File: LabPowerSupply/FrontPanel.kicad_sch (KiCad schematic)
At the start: 27 parts

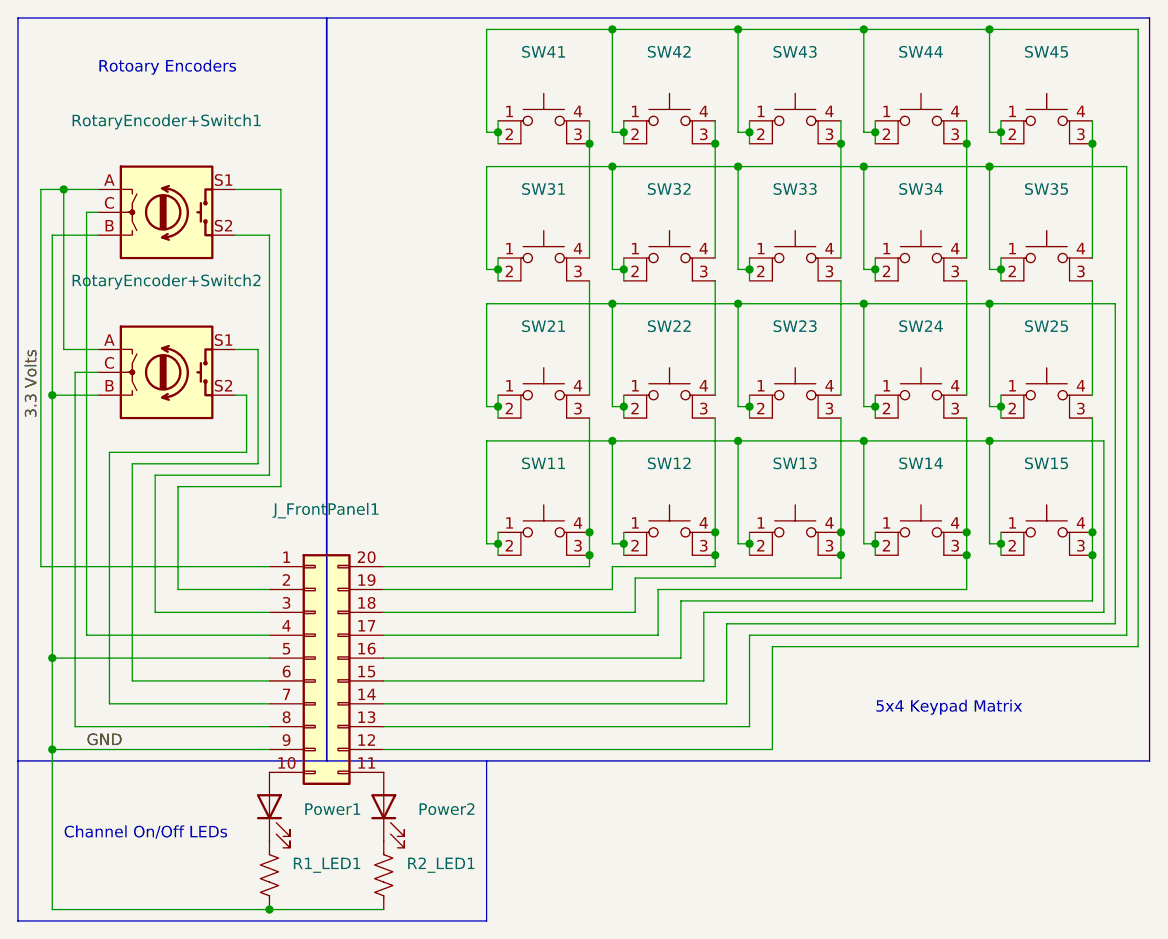
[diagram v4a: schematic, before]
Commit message: Added mcu capacitors, split 5v inductors
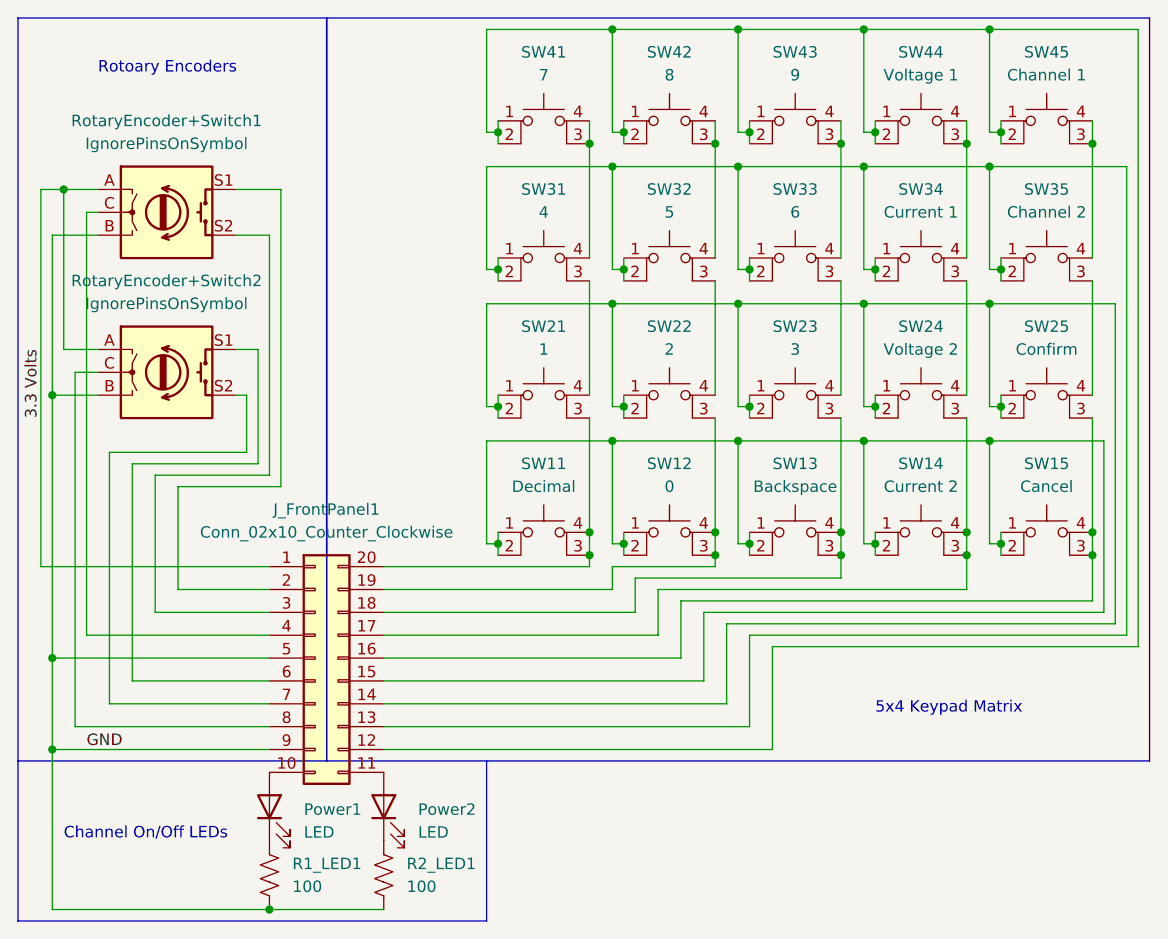
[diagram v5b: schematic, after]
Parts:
- J_FrontPanel1: value (none) -> Conn_02x10_Counter_Clockwise; footprint (none) -> Connector_IDC:IDC-Header_2x10_P2.54mm_Vertical
- Power1, Power2: value (none) -> LED; footprint (none) -> LED_THT:LED_D3.0mm
- R1_LED1, R2_LED1: value (none) -> 100; footprint (none) -> Resistor_SMD:R_0603_1608Metric
- RotaryEncoder+Switch1, RotaryEncoder+Switch2: value (none) -> IgnorePinsOnSymbol; footprint (none) -> Rotary_Encoder:RotaryEncoder_Alps_EC11E-Switch_Vertical_H20mm
- SW11: value (none) -> Decimal; footprint (none) -> Button_Switch_SMD:SW_MEC_5GSH9
- SW12: value (none) -> 0; footprint (none) -> Button_Switch_SMD:SW_MEC_5GSH9
- SW13: value (none) -> Backspace; footprint (none) -> Button_Switch_SMD:SW_MEC_5GSH9
- SW14: value (none) -> Current 2; footprint (none) -> Button_Switch_SMD:SW_MEC_5GSH9
- SW15: value (none) -> Cancel; footprint (none) -> Button_Switch_SMD:SW_MEC_5GSH9
- SW21: value (none) -> 1; footprint (none) -> Button_Switch_SMD:SW_MEC_5GSH9
- SW22: value (none) -> 2; footprint (none) -> Button_Switch_SMD:SW_MEC_5GSH9
- SW23: value (none) -> 3; footprint (none) -> Button_Switch_SMD:SW_MEC_5GSH9
- SW24: value (none) -> Voltage 2; footprint (none) -> Button_Switch_SMD:SW_MEC_5GSH9
- SW25: value (none) -> Confirm; footprint (none) -> Button_Switch_SMD:SW_MEC_5GSH9
- SW31: value (none) -> 4; footprint (none) -> Button_Switch_SMD:SW_MEC_5GSH9
- SW32: value (none) -> 5; footprint (none) -> Button_Switch_SMD:SW_MEC_5GSH9
- SW33: value (none) -> 6; footprint (none) -> Button_Switch_SMD:SW_MEC_5GSH9
- SW34: value (none) -> Current 1; footprint (none) -> Button_Switch_SMD:SW_MEC_5GSH9
- SW35: value (none) -> Channel 2; footprint (none) -> Button_Switch_SMD:SW_MEC_5GSH9
- SW41: value (none) -> 7; footprint (none) -> Button_Switch_SMD:SW_MEC_5GSH9
- SW42: value (none) -> 8; footprint (none) -> Button_Switch_SMD:SW_MEC_5GSH9
- SW43: value (none) -> 9; footprint (none) -> Button_Switch_SMD:SW_MEC_5GSH9
- SW44: value (none) -> Voltage 1; footprint (none) -> Button_Switch_SMD:SW_MEC_5GSH9
- SW45: value (none) -> Channel 1; footprint (none) -> Button_Switch_SMD:SW_MEC_5GSH9

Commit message: Start tallying
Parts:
- removed J_FrontPanel1: Conn_02x10_Counter_Clockwise, Connector_IDC:IDC-Header_2x10_P2.54mm_Vertical, symbol Connector_Generic:Conn_02x10_Counter_Clockwise
- removed R2_LED1: 100, Resistor_SMD:R_0603_1608Metric, symbol Device:R_US
- removed RotaryEncoder+Switch2: IgnorePinsOnSymbol, Rotary_Encoder:RotaryEncoder_Alps_EC11E-Switch_Vertical_H20mm, symbol Device:RotaryEncoder_Switch
- added J_FrontPanel2: Conn_02x10_Counter_Clockwise, Connector_IDC:IDC-Header_2x10_P2.54mm_Vertical, symbol Connector_Generic:Conn_02x08_Counter_Clockwise
- added R1_LED2: 100, Resistor_SMD:R_0603_1608Metric, symbol Device:R_US
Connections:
- net 3.3 Volts: now also J_FrontPanel2.1 (Pin_1)
- net at SW31.1, SW31.2, SW32.1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: now also J_FrontPanel2.9 (Pin_9)
- net at SW11.1, SW11.2, SW12.1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: now also J_FrontPanel2.11 (Pin_11)
- net at SW12.3 (K), SW12.4 (A), SW22.3 (K): now also J_FrontPanel2.15 (Pin_15)
- net at Power1.2 (A): now also J_FrontPanel2.6 (Pin_6)
- net at Power2.2 (A): now also J_FrontPanel2.7 (Pin_7)
- net at SW41.1, SW41.2, SW42.1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: now also J_FrontPanel2.8 (Pin_8)
- net at SW21.1, SW21.2, SW22.1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: now also J_FrontPanel2.10 (Pin_10)
- net at SW15.3 (K), SW15.4 (A), SW25.3 (K): now also J_FrontPanel2.12 (Pin_12)
- net at SW14.3 (K), SW14.4 (A), SW24.3 (K): now also J_FrontPanel2.13 (Pin_13)
- net at SW13.3 (K), SW13.4 (A), SW23.3 (K): now also J_FrontPanel2.14 (Pin_14)
- net at RotaryEncoder+Switch1.S1: now also J_FrontPanel2.2 (Pin_2)
- net at SW11.3 (K), SW11.4 (A), SW21.3 (K): now also J_FrontPanel2.16 (Pin_16)
- net at RotaryEncoder+Switch1.S2: now also J_FrontPanel2.3 (Pin_3)
- net at RotaryEncoder+Switch1.C: now also J_FrontPanel2.4 (Pin_4)
- net at Power2.1 (K): now also R1_LED2.1
- net GND: no longer names the net of R1_LED1.2, RotaryEncoder+Switch1.B
- net GND: now also J_FrontPanel2.5 (Pin_5), R1_LED2.2
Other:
- note removed: "Channel On/Off LEDs"

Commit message: almost done
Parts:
- renumbered J_FrontPanel2 to FrontPanel2
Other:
- note added: "Rotoary Encoder and LEDs"
- note removed: "Rotoary Encoders"
- moved on the sheet: RotaryEncoder+Switch1
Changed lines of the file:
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@@
     (stroke (width 0) (type default) (color 0 0 0 0))
   )
-  (wire (pts (xy 88.9 78.74) (xy 88.9 125.73))
+  (wire (pts (xy 88.9 101.6) (xy 88.9 125.73))
     (stroke (width 0) (type default) (color 0 0 0 0))
   )
@@
     (stroke (width 0) (type default) (color 0 0 0 0))
   )
-  (wire (pts (xy 92.71 78.74) (xy 88.9 78.74))
+  (wire (pts (xy 92.71 101.6) (xy 88.9 101.6))
     (stroke (width 0) (type default) (color 0 0 0 0))
   )
@@
     (stroke (width 0) (type default) (color 0 0 0 0))
   )
-  (wire (pts (xy 92.71 76.2) (xy 91.44 76.2))
+  (wire (pts (xy 92.71 99.06) (xy 91.44 99.06))
     (stroke (width 0) (type default) (color 0 0 0 0))
   )
@@
     (stroke (width 0) (type default) (color 0 0 0 0))
   )
-  (wire (pts (xy 107.95 73.66) (xy 113.03 73.66))
+  (wire (pts (xy 107.95 96.52) (xy 113.03 96.52))
     (stroke (width 0) (type default) (color 0 0 0 0))
   )
@@
     (stroke (width 0) (type default) (color 0 0 0 0))
   )
-  (wire (pts (xy 111.76 78.74) (xy 111.76 105.41))
+  (wire (pts (xy 111.76 101.6) (xy 111.76 105.41))
     (stroke (width 0) (type default) (color 0 0 0 0))
   )
@@
     (stroke (width 0) (type default) (color 0 0 0 0))
   )
-  (wire (pts (xy 107.95 78.74) (xy 111.76 78.74))
+  (wire (pts (xy 107.95 101.6) (xy 111.76 101.6))
     (stroke (width 0) (type default) (color 0 0 0 0))
   )
@@
     (stroke (width 0) (type default) (color 0 0 0 0))
   )
-  (wire (pts (xy 86.36 73.66) (xy 92.71 73.66))
+  (wire (pts (xy 86.36 96.52) (xy 92.71 96.52))
     (stroke (width 0) (type default) (color 0 0 0 0))
   )
@@
     (stroke (width 0) (type default) (color 0 0 0 0))
   )
-  (wire (pts (xy 86.36 115.57) (xy 86.36 73.66))
+  (wire (pts (xy 86.36 115.57) (xy 86.36 96.52))
     (stroke (width 0) (type default) (color 0 0 0 0))
   )
@@
     (stroke (width 0) (type default) (color 0 0 0 0))
   )
-  (wire (pts (xy 113.03 73.66) (xy 113.03 106.68))
+  (wire (pts (xy 113.03 96.52) (xy 113.03 106.68))
     (stroke (width 0) (type default) (color 0 0 0 0))
   )
@@
     (stroke (width 0) (type default) (color 0 0 0 0))
   )
-  (wire (pts (xy 91.44 76.2) (xy 91.44 123.19))
+  (wire (pts (xy 91.44 99.06) (xy 91.44 123.19))
     (stroke (width 0) (type default) (color 0 0 0 0))
   )
@@
     (stroke (width 0) (type default) (color 0 0 0 0))
   )
-  (text "Rotoary Encoders" (at 92.71 60.96 0)
+  (text "Rotoary Encoder and LEDs" (at 87.63 83.82 0)
     (effects (font (size 1.27 1.27)) (justify left bottom))
   )
@@
   (symbol (lib_id "Connector_Generic:Conn_02x08_Counter_Clockwise") (at 116.84 123.19 0) (unit 1)
     (in_bom yes) (on_board yes)
-    (property "Reference" "J_FrontPanel2" (id 0) (at 118.11 109.22 0))
+    (property "Reference" "FrontPanel2" (id 0) (at 118.11 109.22 0))
     (property "Value" "Conn_02x10_Counter_Clockwise" (id 1) (at 118.11 111.76 0))
     (property "Footprint" "Connector_IDC:IDC-Header_2x10_P2.54mm_Vertical" (id 2) (at 116.84 123.19 0)
@@
     (pin "4")
   )
-  (symbol (lib_id "Device:RotaryEncoder_Switch") (at 100.33 76.2 0) (unit 1)
-    (in_bom yes) (on_board yes) (fields_autoplaced)
-    (property "Reference" "RotaryEncoder+Switch1" (id 0) (at 100.33 66.04 0))
-    (property "Value" "IgnorePinsOnSymbol" (id 1) (at 100.33 68.58 0))
-    (property "Footprint" "Rotary_Encoder:RotaryEncoder_Alps_EC11E-Switch_Vertical_H20mm" (id 2) (at 96.52 72.136 0)
-      (effects (font (size 1.27 1.27)) hide)
-    )
-    (property "Datasheet" "~" (id 3) (at 100.33 69.596 0)
-      (effects (font (size 1.27 1.27)) hide)
-    )
+  (symbol (lib_id "Device:RotaryEncoder_Switch") (at 100.33 99.06 0) (unit 1)
+    (in_bom yes) (on_board yes) (fields_autoplaced)
+    (property "Reference" "RotaryEncoder+Switch1" (id 0) (at 100.33 88.9 0))
+    (property "Value" "IgnorePinsOnSymbol" (id 1) (at 100.33 91.44 0))
+    (property "Footprint" "Rotary_Encoder:RotaryEncoder_Alps_EC11E-Switch_Vertical_H20mm" (id 2) (at 96.52 94.996 0)
+      (effects (font (size 1.27 1.27)) hide)
+    )
+    (property "Datasheet" "~" (id 3) (at 100.33 92.456 0)
+      (effects (font (size 1.27 1.27)) hide)
+    )

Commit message: Update pcb footprints
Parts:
- renumbered FrontPanel2 to FrontPanel1
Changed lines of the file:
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@@
   (symbol (lib_id "Connector_Generic:Conn_02x08_Counter_Clockwise") (at 116.84 123.19 0) (unit 1)
     (in_bom yes) (on_board yes)
-    (property "Reference" "FrontPanel2" (id 0) (at 118.11 109.22 0))
+    (property "Reference" "FrontPanel1" (id 0) (at 118.11 109.22 0))
     (property "Value" "Conn_02x10_Counter_Clockwise" (id 1) (at 118.11 111.76 0))
     (property "Footprint" "Connector_IDC:IDC-Header_2x10_P2.54mm_Vertical" (id 2) (at 116.84 123.19 0)
